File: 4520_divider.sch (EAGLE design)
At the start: 54 parts, among them IC1 4520N, IC2 4050N, IC3 78L05Z

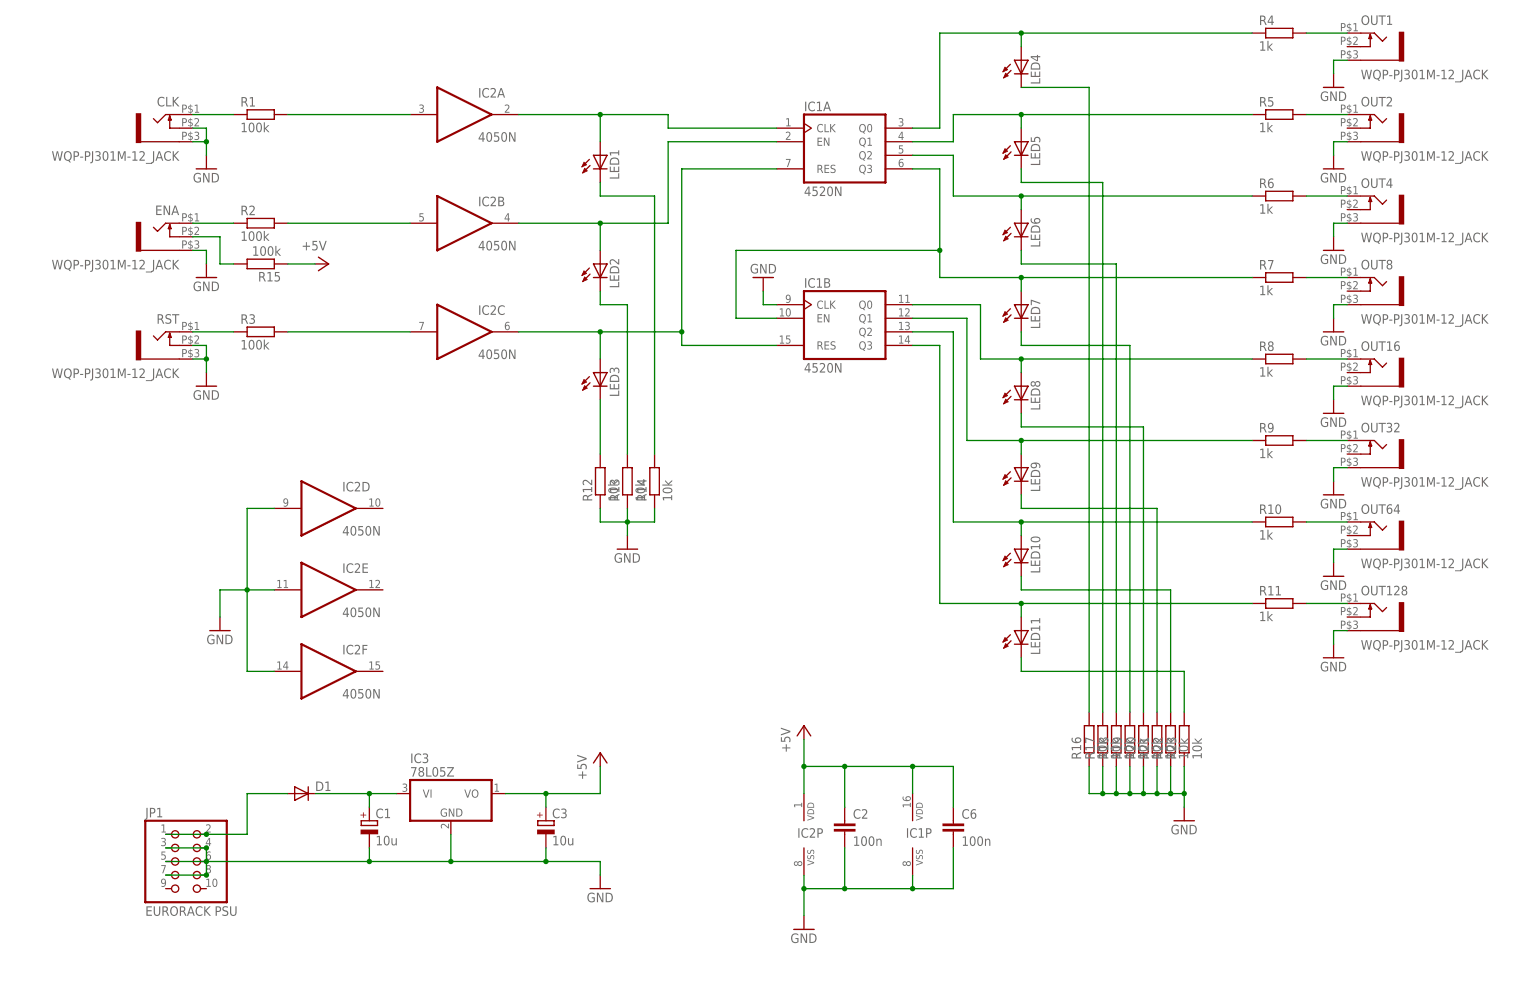
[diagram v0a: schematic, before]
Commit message: Moved a few resistors for clarity.
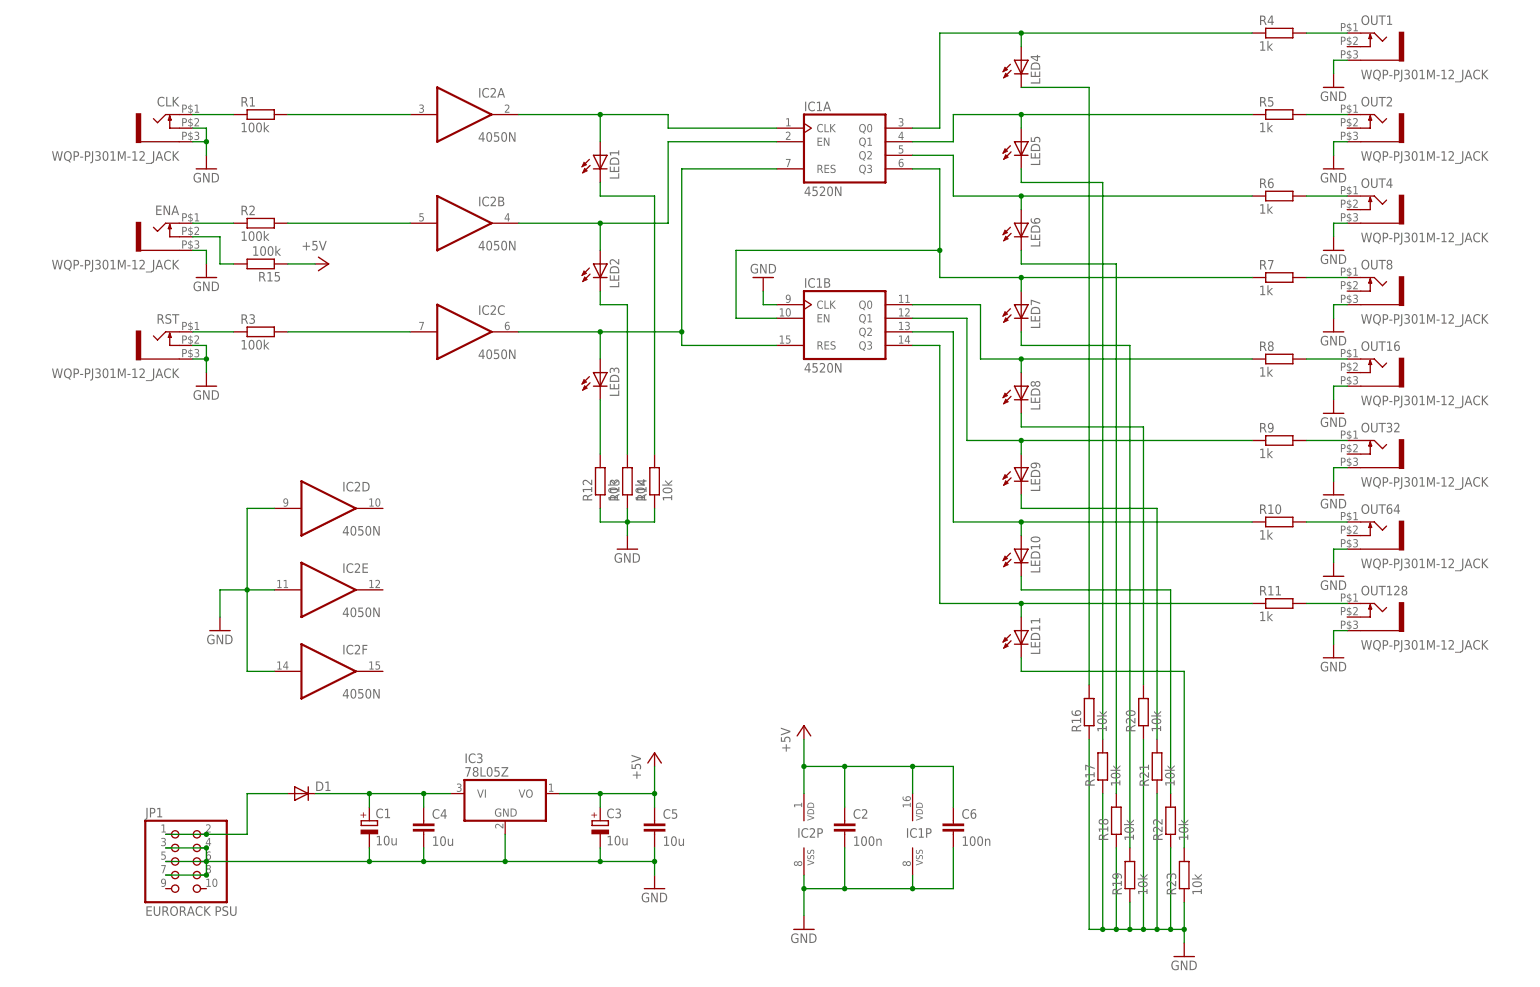
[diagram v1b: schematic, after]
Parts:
- added C4, C5: 10u, rcl:C-EUC1206K
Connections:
- net +5V: now also C5.1
- net GND: now also C4.2, C5.2
- net N$7: now also C4.1
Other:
- moved on the sheet: C3, IC3, R16, R17, R18, R19, R20, R21, R22, R23
